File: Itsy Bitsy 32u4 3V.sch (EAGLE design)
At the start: 23 parts, among them IC1 ATMEGA32U4-MU, IC2 74HCT1G125DBV, SW1 SPST_TACT-KMR2, U2 MIC5225-3.3, X3 microUSB, Y1 8MHz

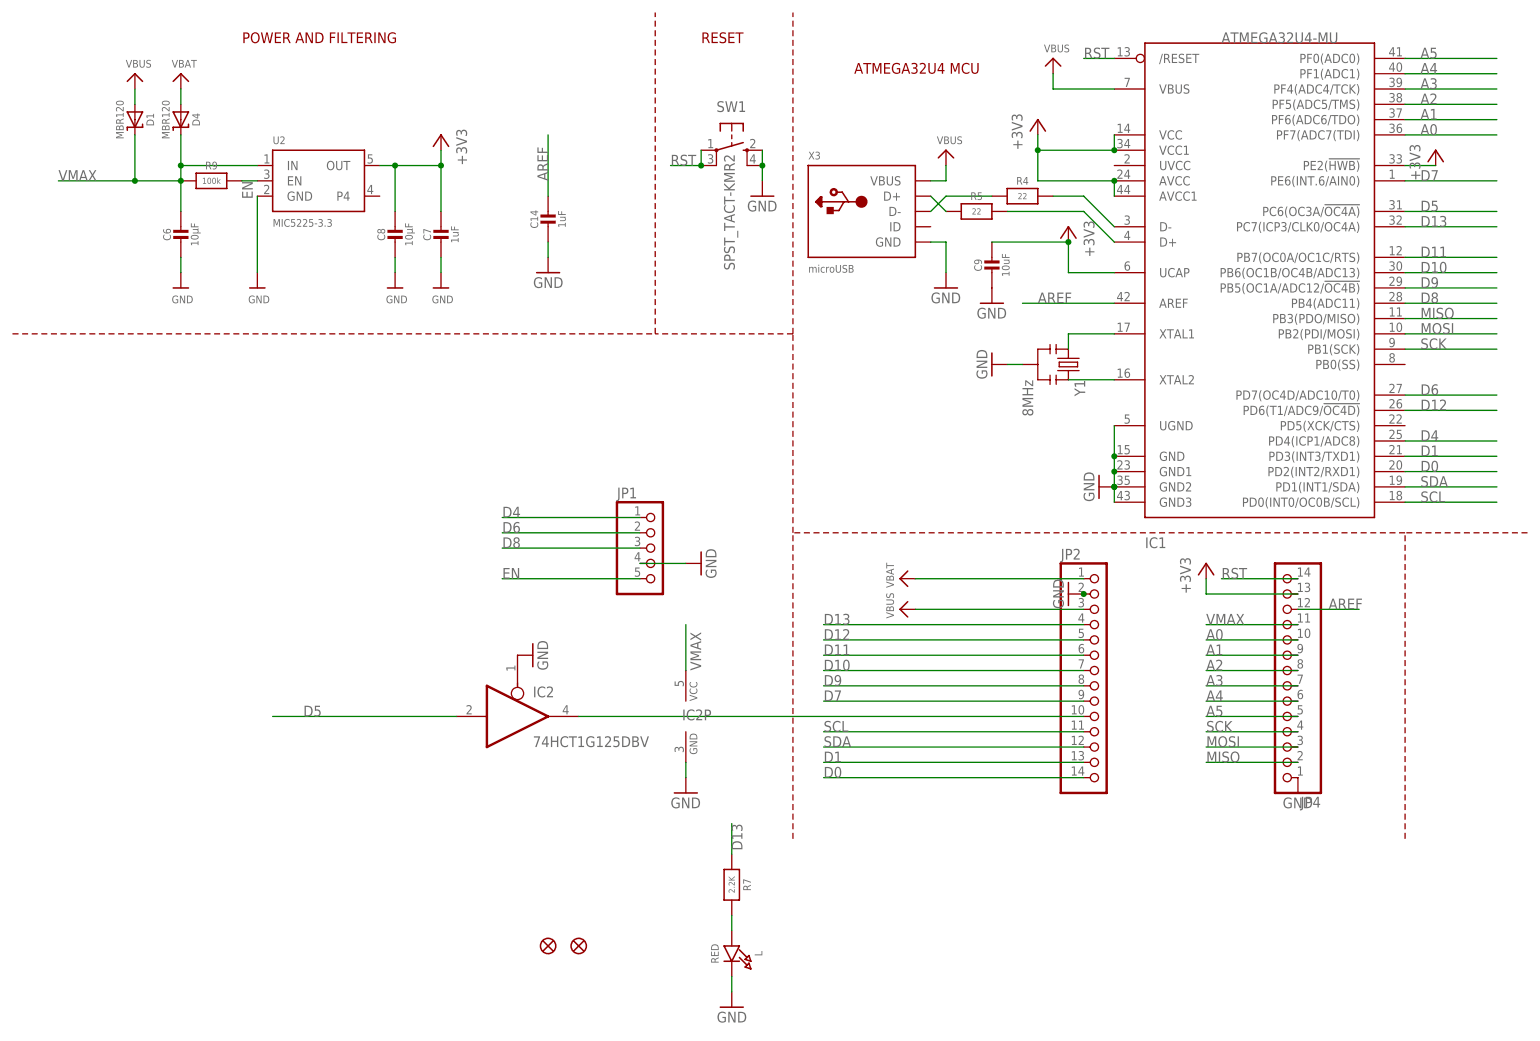
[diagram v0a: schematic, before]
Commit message: update 3V regulator label
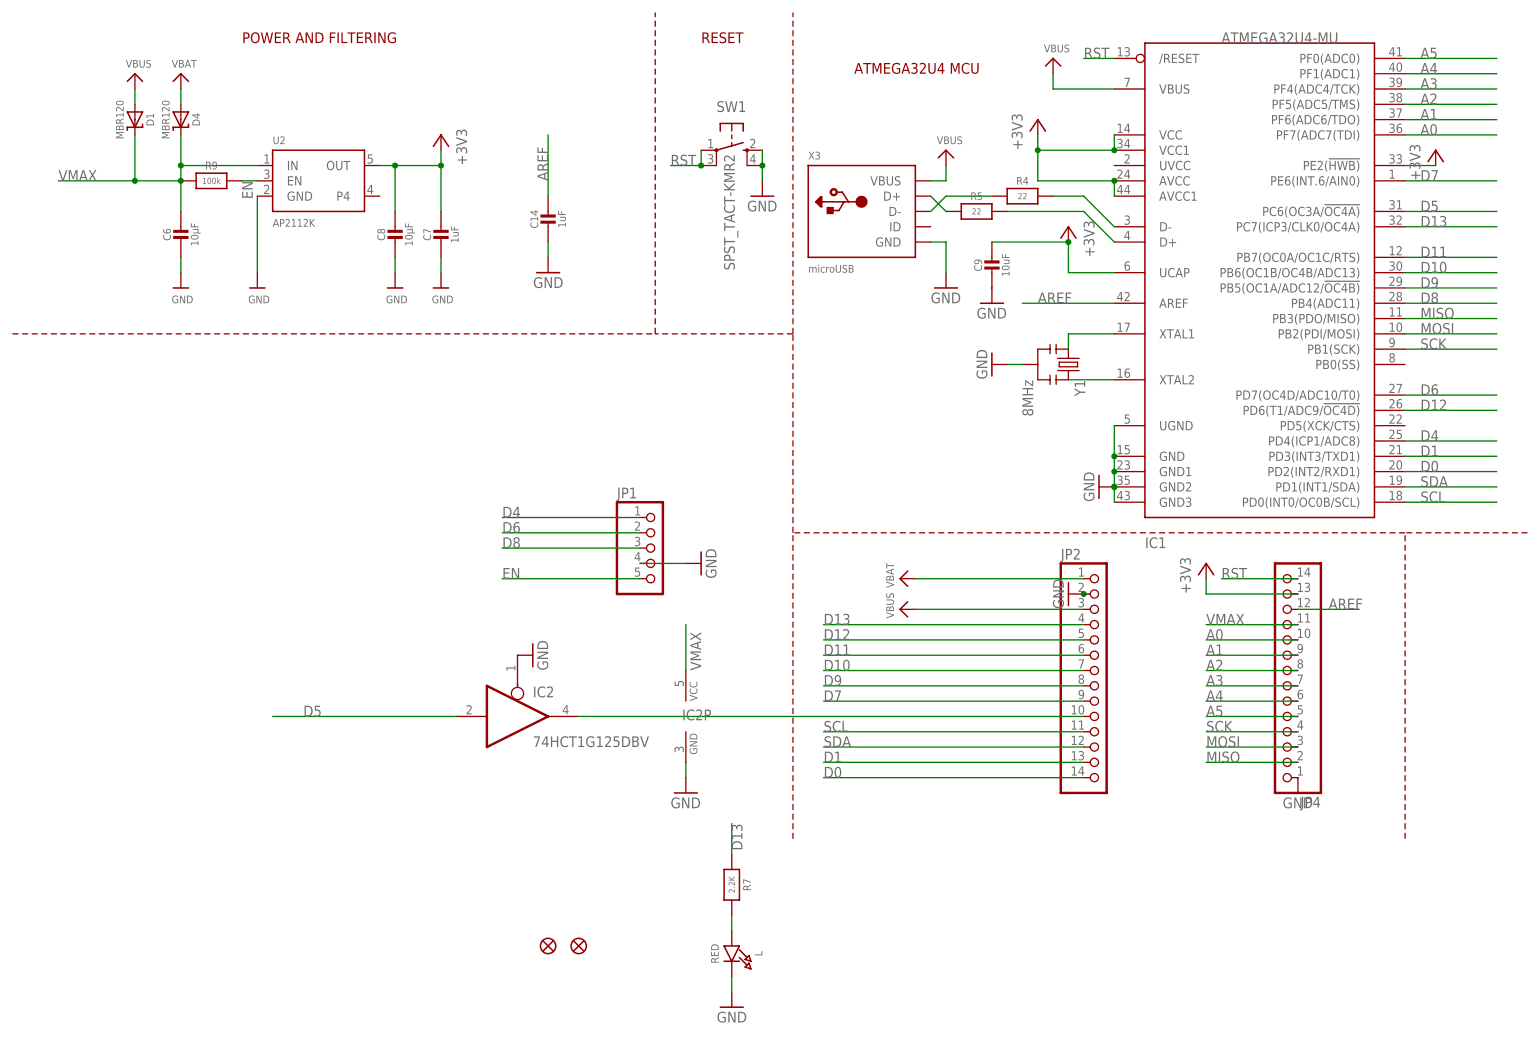
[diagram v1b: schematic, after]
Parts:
- U2: value MIC5225-3.3 -> AP2112K
